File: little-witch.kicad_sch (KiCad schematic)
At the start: 39 parts, among them J3 Conn_ARM_SWD_TagConnect_TC203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, J4 GCT-USB4105, J5 Conn_02x20_Odd_Even, J6 USB1, SW1 RESET, SW2 BOOT0, U1 CH32V307RCT6, U4 LM66100DCK, Y1 SIT8008BI-73-33N-25.000000

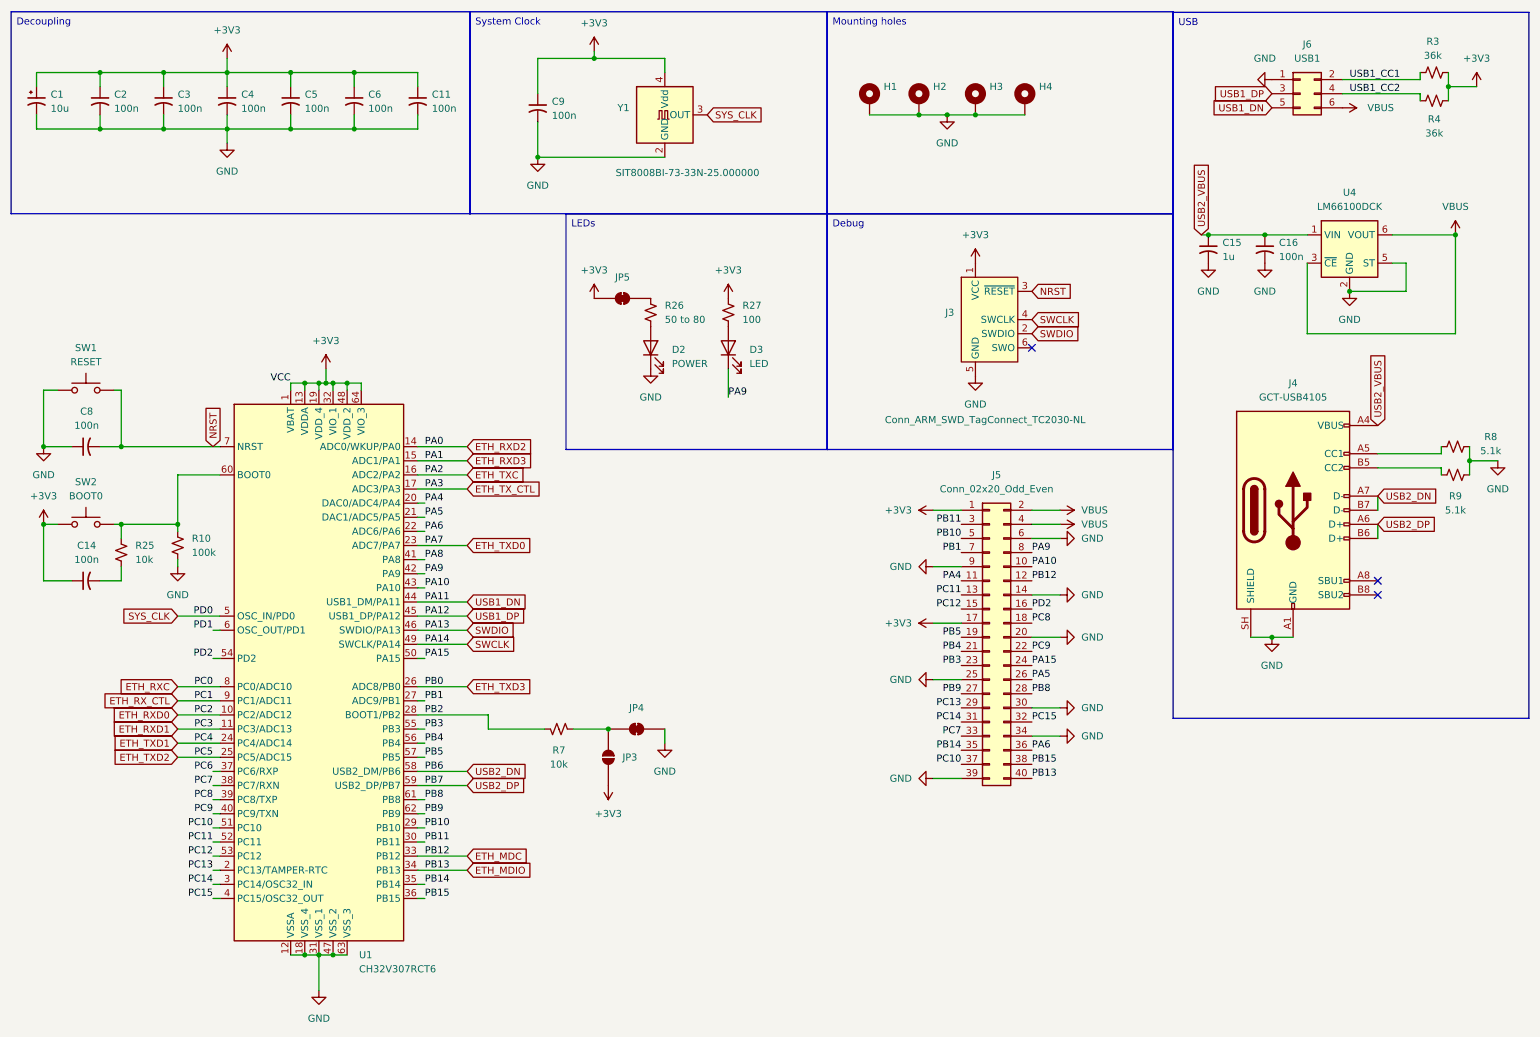
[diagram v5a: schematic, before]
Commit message: v0.3.0 with gpio routing, updated labeling, leds
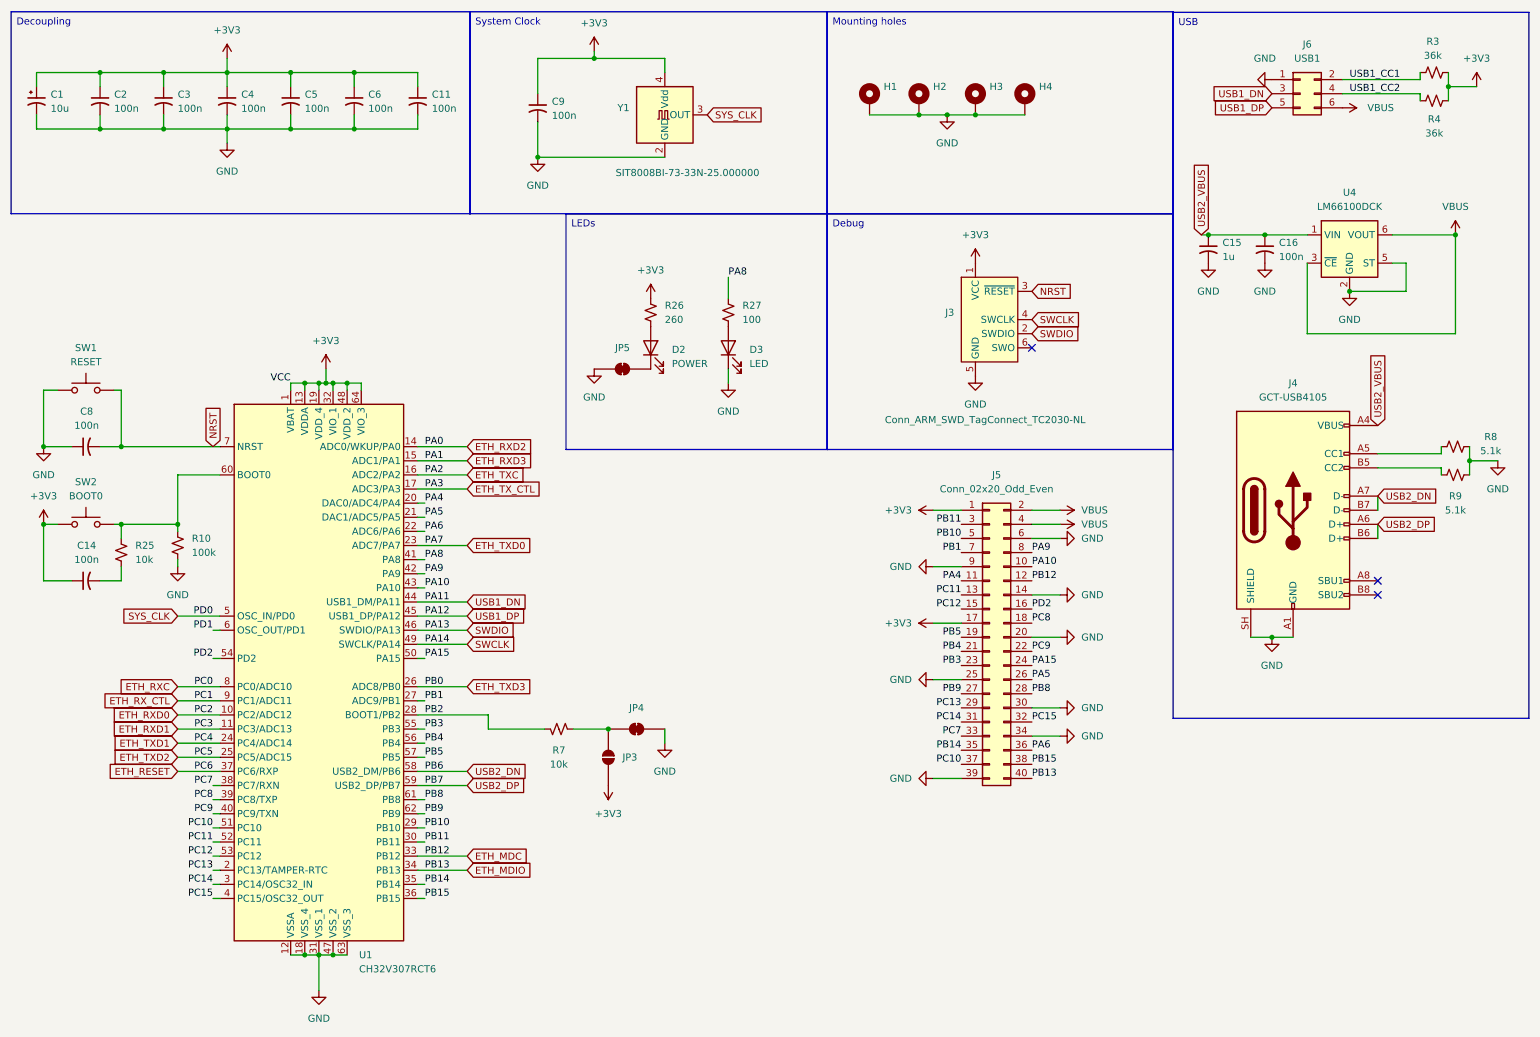
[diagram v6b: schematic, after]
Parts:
- JP5: value SolderJumper_2_Open -> P. LED
- R26: value 50 to 80 -> 260
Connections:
- net +3V3: now also R26.2; no longer JP5.1 (A), R27.2
- net GND: now also D3.1 (K), JP5.1 (A); no longer D2.1 (K)
- net PA8: now also R27.2
- net PA9: no longer D3.1 (K)
- net USB1_DN: now also J6.3 (Pin_3); no longer J6.5 (Pin_5)
- net USB1_DP: now also J6.5 (Pin_5); no longer J6.3 (Pin_3)
- net at JP5.2 (B): now also D2.1 (K); no longer R26.2
- net PC6 renamed ETH_RESET

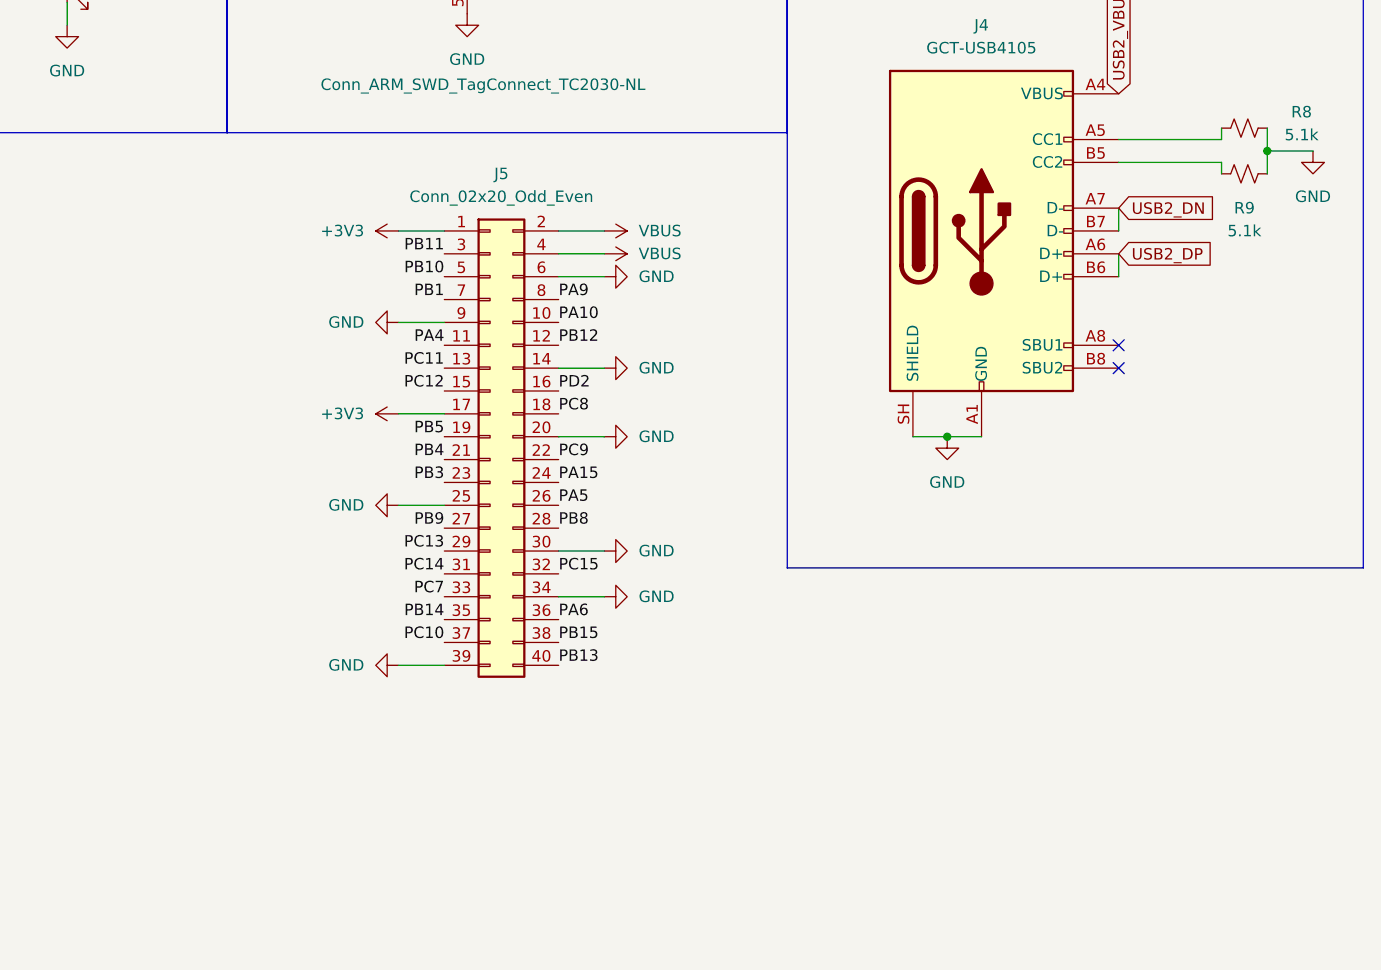
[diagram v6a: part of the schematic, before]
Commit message: PCM multiplexing before USB rework
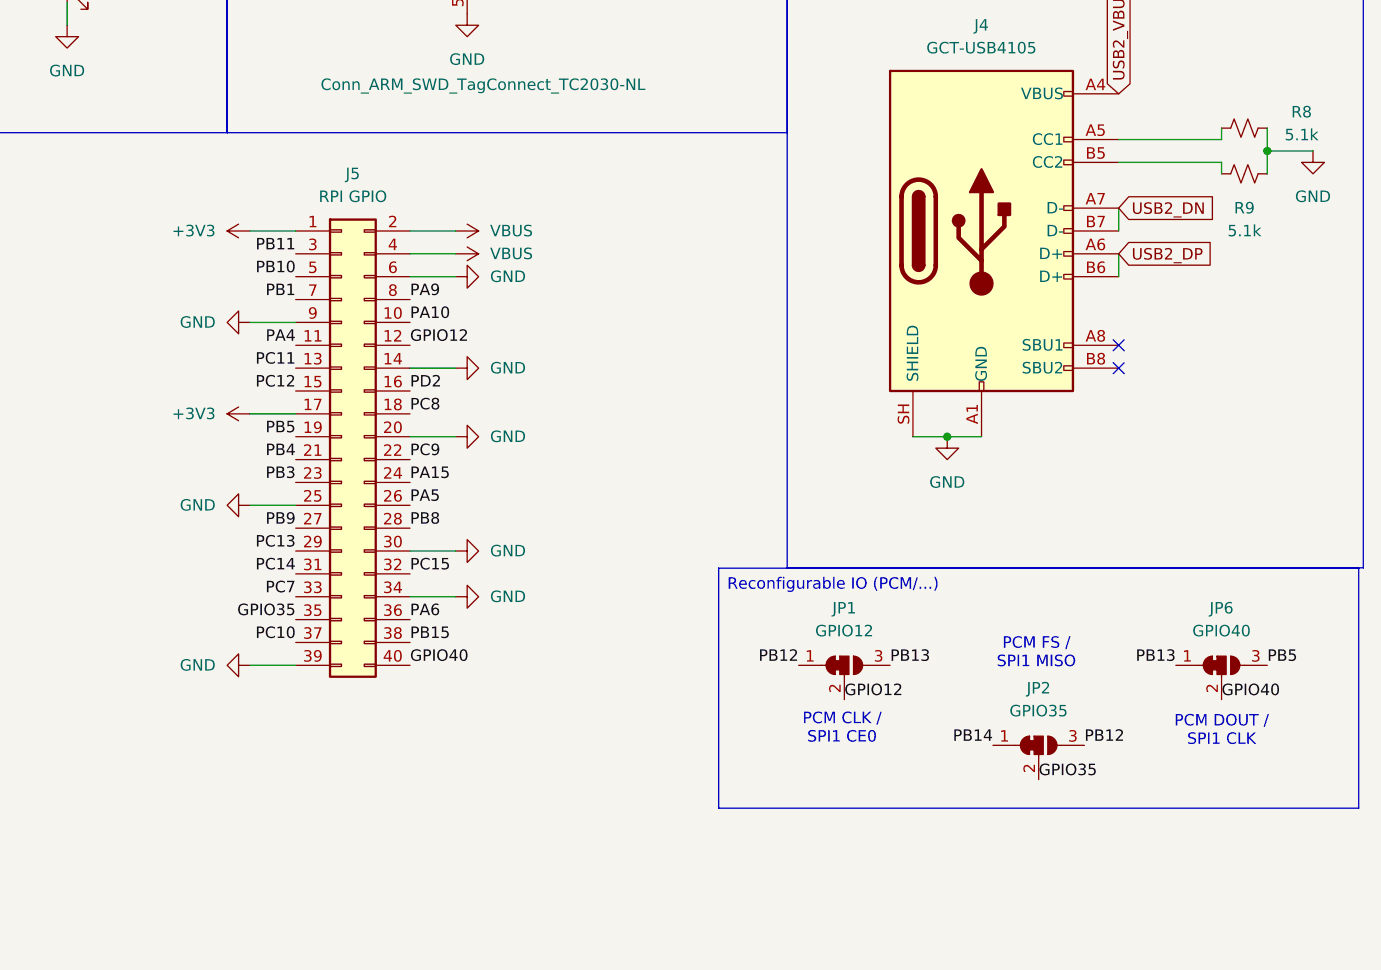
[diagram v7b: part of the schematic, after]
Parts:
- added JP1: GPIO12, Jumper:SolderJumper-3_P1.3mm_Bridged12_RoundedPad1.0x1.5mm_NumberLabels, symbol Jumper:SolderJumper_3_Bridged12
- added JP2: GPIO35, Jumper:SolderJumper-3_P1.3mm_Bridged12_RoundedPad1.0x1.5mm_NumberLabels, symbol Jumper:SolderJumper_3_Bridged12
- added JP6: GPIO40, Jumper:SolderJumper-3_P1.3mm_Bridged12_RoundedPad1.0x1.5mm_NumberLabels, symbol Jumper:SolderJumper_3_Bridged12
- J5: value Conn_02x20_Odd_Even -> RPI GPIO
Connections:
- net ETH_MDC: now also JP1.1 (A), JP2.3 (B); no longer J5.12 (Pin_12)
- net ETH_MDIO: now also JP1.3 (B), JP6.1 (A); no longer J5.40 (Pin_40)
- net PB14: now also JP2.1 (A); no longer J5.35 (Pin_35)
- net PB5: now also JP6.3 (B)
- new net GPIO12: J5.12 (Pin_12), JP1.2 (C)
- new net GPIO35: J5.35 (Pin_35), JP2.2 (C)
- new net GPIO40: J5.40 (Pin_40), JP6.2 (C)
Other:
- note added: "PCM CLK / SPI1 CE0"
- note added: "PCM DOUT / SPI1 CLK"
- note added: "PCM FS / SPI1 MISO"
- moved on the sheet: J5

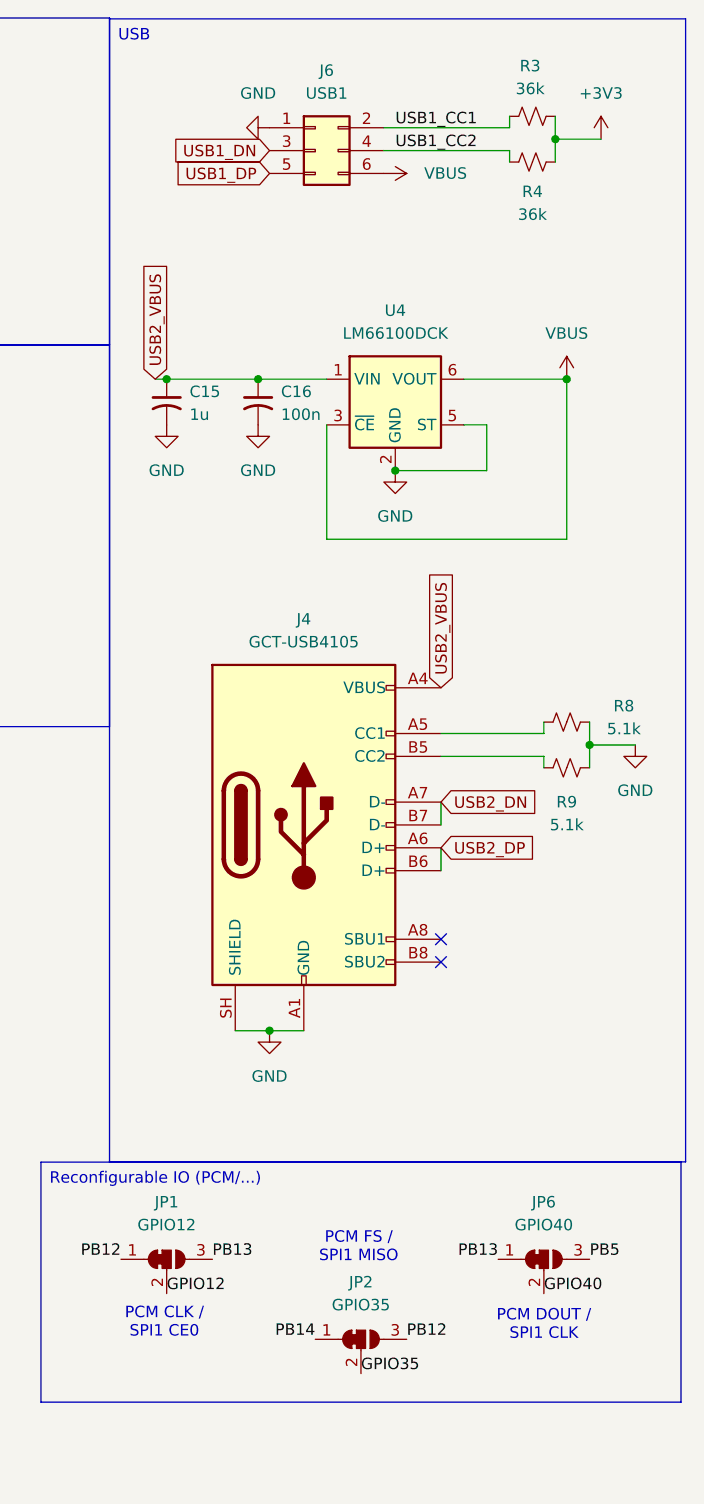
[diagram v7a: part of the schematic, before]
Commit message: PCM multiplexing routing done
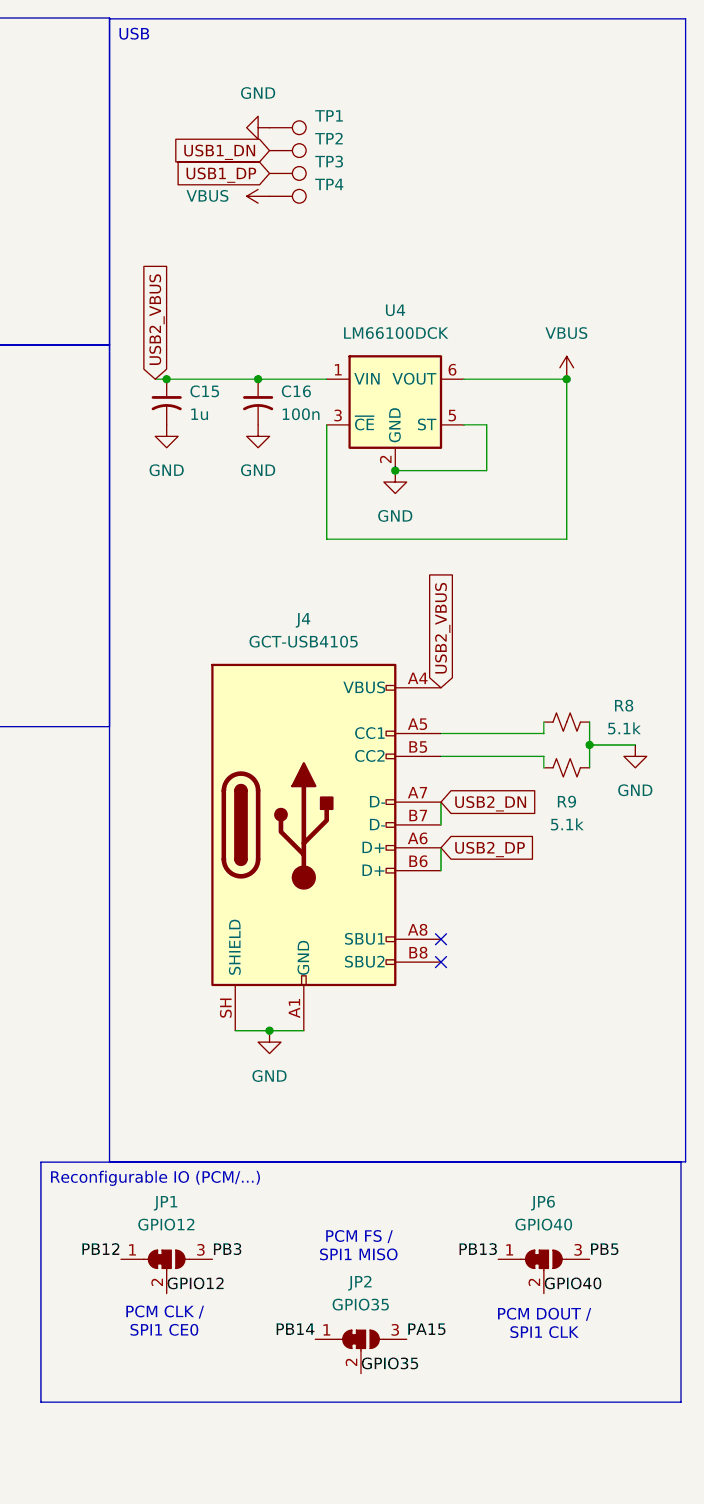
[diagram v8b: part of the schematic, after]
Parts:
- removed J6: USB1, Connector_PinSocket_1.27mm:PinSocket_2x03_P1.27mm_Vertical, symbol Connector_Generic:Conn_02x03_Odd_Even
- removed R3, R4: 36k, Resistor_SMD:R_0402_1005Metric, symbol Device:R_Small_US
- added TP1, TP4: TestPoint, TestPoint:TestPoint_Pad_D2.0mm, symbol Connector:TestPoint
- added TP2, TP3: TestPoint, TestPoint:TestPoint_Pad_D1.5mm, symbol Connector:TestPoint
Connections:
- net ETH_MDC: no longer JP2.3 (B)
- net ETH_MDIO: no longer JP1.3 (B)
- net GND: now also TP1.1
- net PA15: now also JP2.3 (B)
- net PB3: now also JP1.3 (B)
- net USB1_DN: now also TP2.1
- net USB1_DP: now also TP3.1
- net VBUS: now also TP4.1
